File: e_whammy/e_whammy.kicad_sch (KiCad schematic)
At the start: 15 parts, among them J1 I/O connector, U1 HT7550-1, U2 TLV6001UIDBVR, U3 DRV5056

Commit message: Added kikit fab script
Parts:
- RV1: JLCPCB_CORRECTION (none) -> 0;0;270
- U3: JLCPCB_CORRECTION (none) -> 0;0;180
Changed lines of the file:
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@@
       (effects (font (size 1.524 1.524)) hide)
+    )
+    (property "JLCPCB_CORRECTION" "0;0;270" (id 5) (at 117.475 93.98 0)
+      (effects (font (size 1.27 1.27)) hide)
     )
     (pin "1")
@@
       (effects (font (size 1.524 1.524)) hide)
     )
+    (property "JLCPCB_CORRECTION" "0;0;180" (id 5) (at 107.95 118.11 0)
+      (effects (font (size 1.27 1.27)) hide)
+    )
     (pin "1")

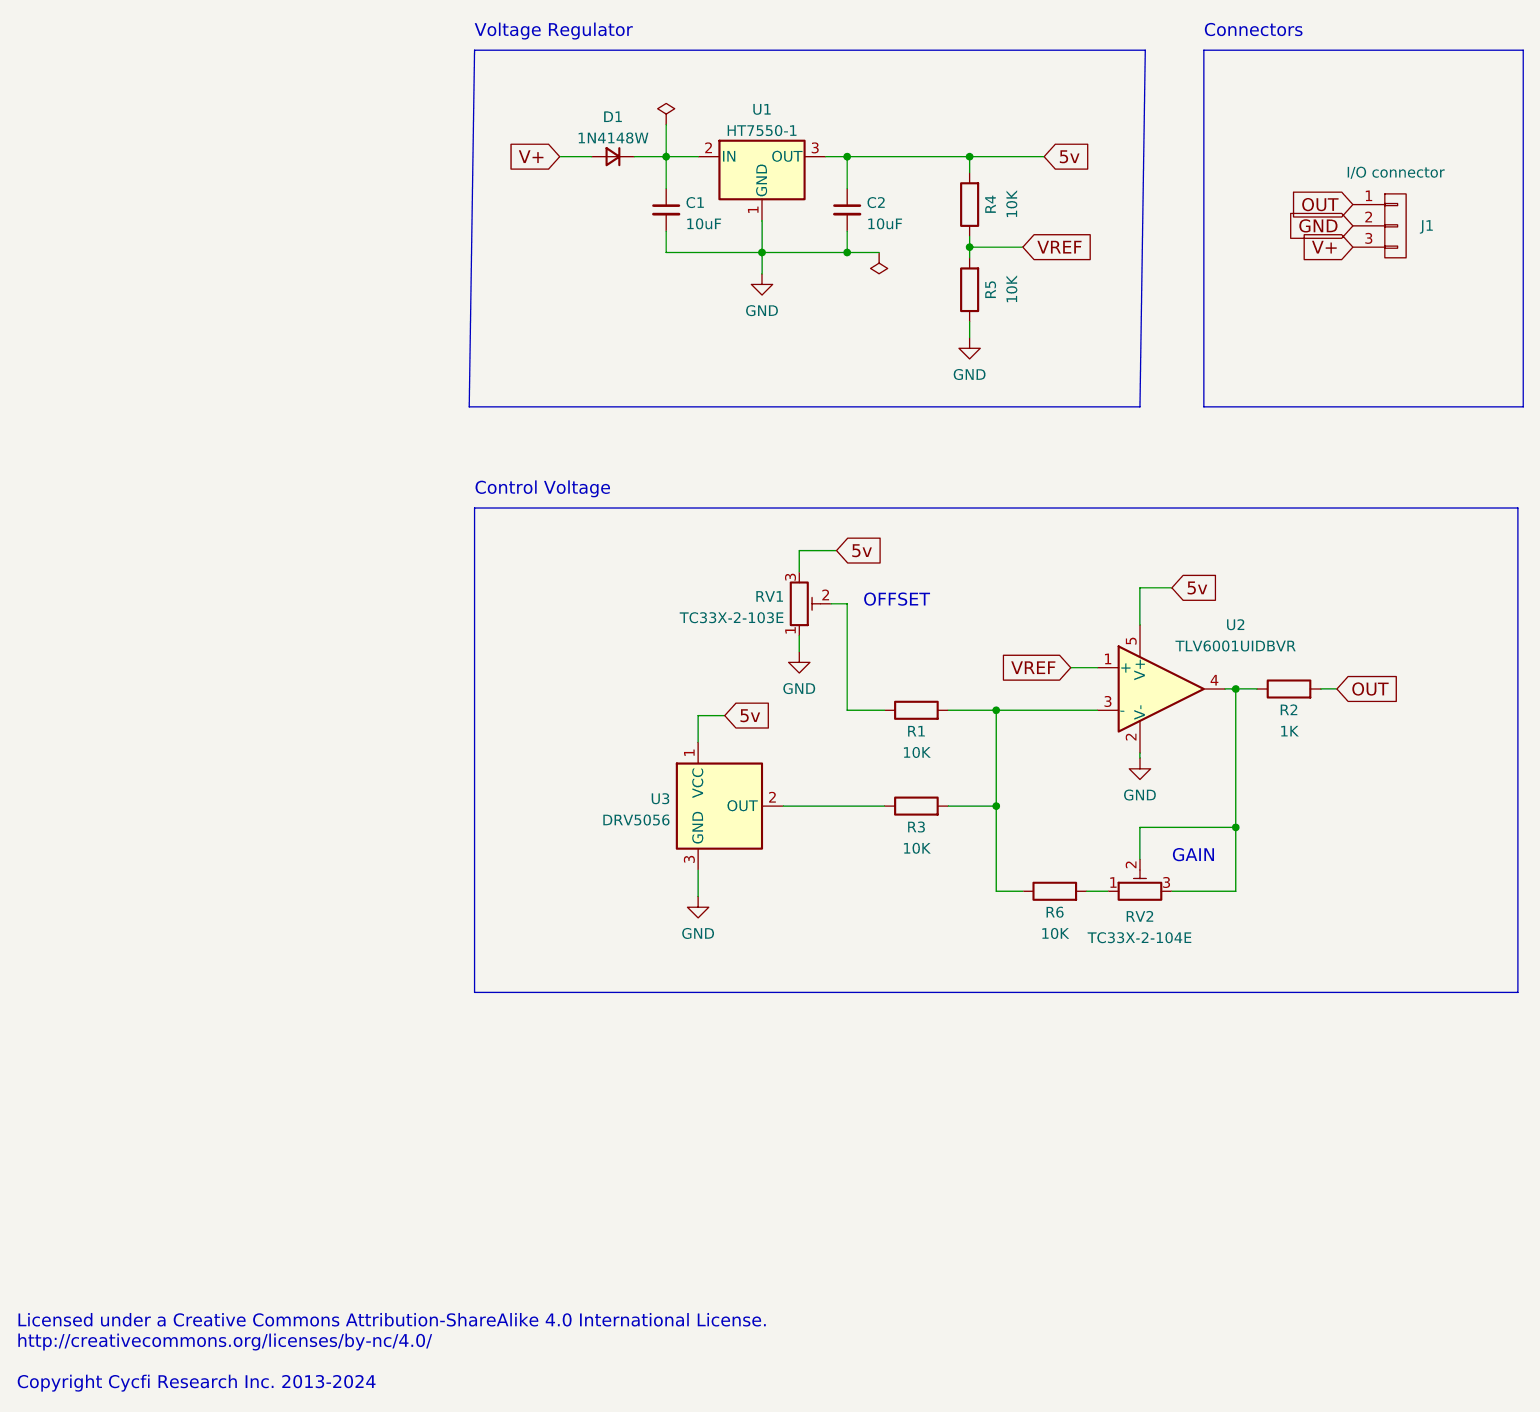
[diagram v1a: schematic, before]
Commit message: Changed to non-inverting configuration
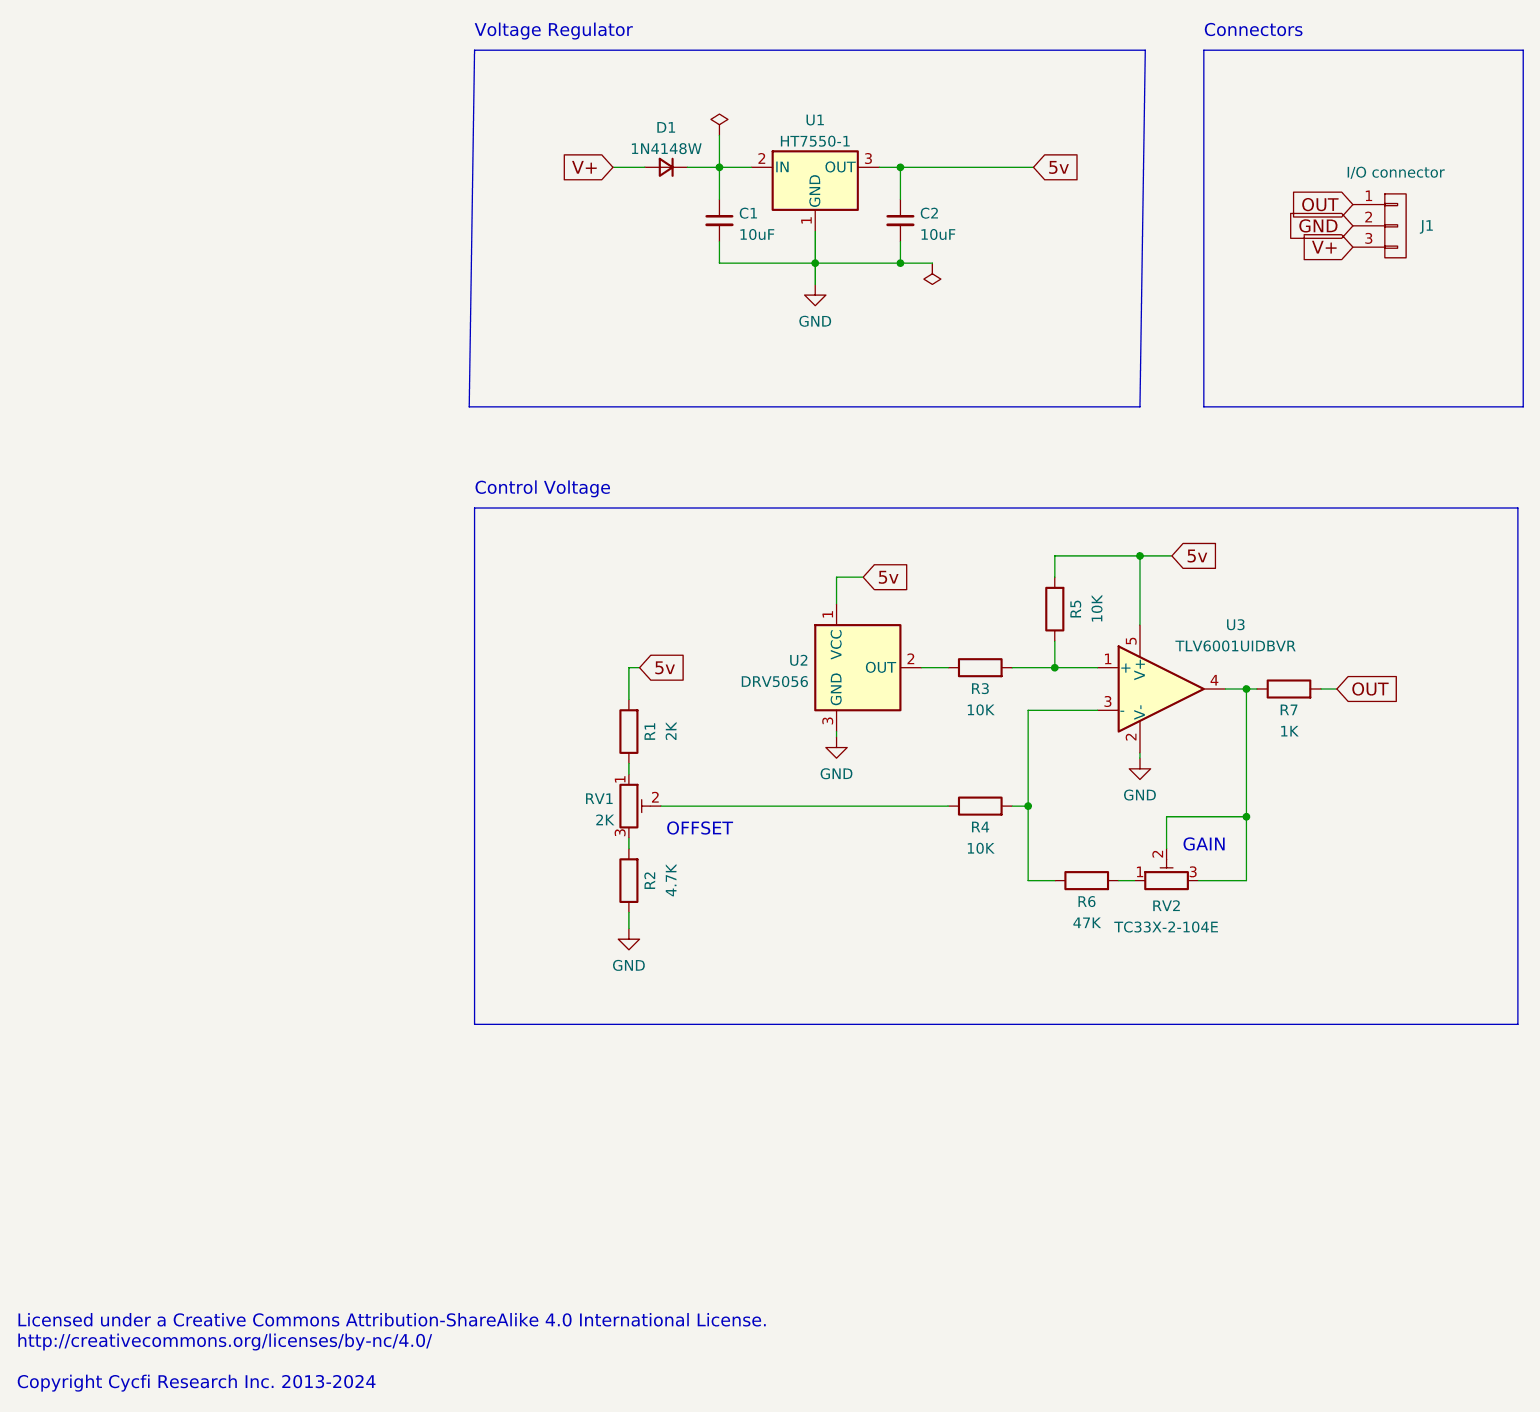
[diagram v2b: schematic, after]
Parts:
- removed R5: 10K, Resistor_SMD:R_0402_1005Metric, symbol Device:R
- added R1: 2K, Resistor_SMD:R_0402_1005Metric, symbol Device:R
- added R6: 47K, Resistor_SMD:R_0402_1005Metric, symbol Device:R
- R2: renamed from R6; value 10K -> 4.7K; LCSC C25744 -> C25900
- RV1: value TC33X-2-103E -> 2K; LCSC C719176 -> C720647
- renumbered R1 to R5, R2 to R7, U3 to U2, U2 to U3
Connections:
- net 5v: now also R5.2, R1.2; no longer R4.2, RV1.3
- net GND: now also R2.1; no longer RV1.1
- net at R5.1: now also R3.2, U3.1 (+); no longer RV1.2
- net at R2.2: now also RV1.3; no longer RV2.1
- net VREF: no longer names the net of R4.1
- net VREF: now also RV1.2; no longer U3.1 (+)
- new net: R1.1, RV1.1
- new net: R6.2, RV2.1
- new net: R4.2, R6.1, U3.3 (-)
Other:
- moved on the sheet: C1, C2, D1, R2, R3, R5, RV1, RV2, U1, U2

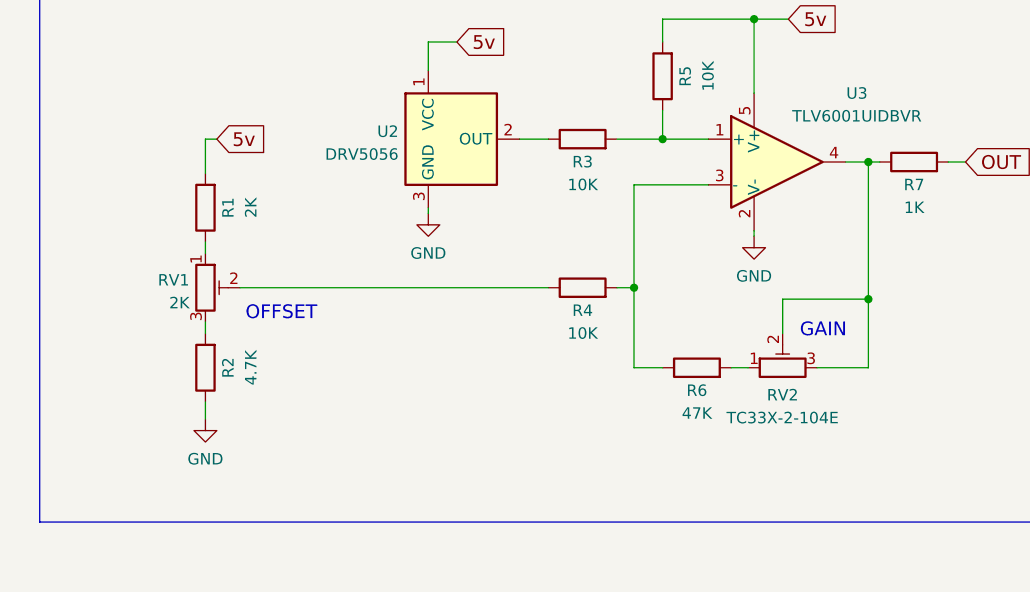
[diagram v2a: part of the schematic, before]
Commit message: Adjusted values for component availability
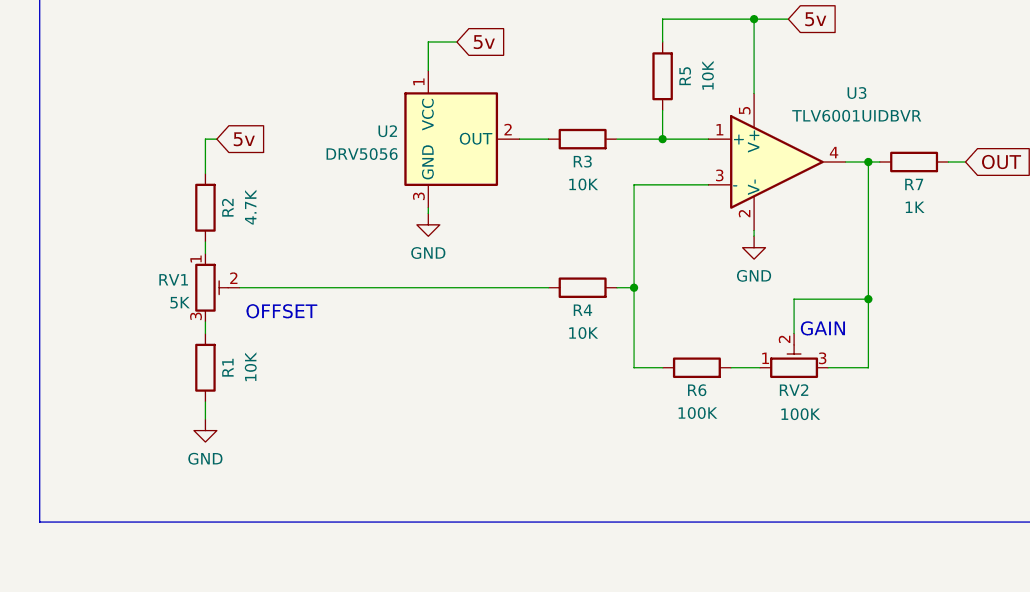
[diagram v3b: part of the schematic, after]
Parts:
- R1: value 2K -> 10K; LCSC C4109 -> C25744
- R6: value 47K -> 100K; LCSC C25792 -> C25741
- RV1: value 2K -> 5K; LCSC C720647 -> C719177
- RV2: value TC33X-2-104E -> 100K
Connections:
- net 5v: now also R2.2; no longer R1.2
- net GND: now also R1.1; no longer R2.1
- net at RV1.1: now also R2.1; no longer R1.1
- net at RV1.3: now also R1.2; no longer R2.2
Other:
- moved on the sheet: R2, RV2
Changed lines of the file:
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@@
   (junction (at 144.78 118.11) (diameter 0) (color 0 0 0 0)
   )
+  (junction (at 119.38 53.34) (diameter 0) (color 0 0 0 0)
+  )
+  (junction (at 129.54 41.91) (diameter 0) (color 0 0 0 0)
+  )
   (junction (at 170.815 119.38) (diameter 0) (color 0 0 0 0)
   )
-  (junction (at 119.38 53.34) (diameter 0) (color 0 0 0 0)
-  )
-  (junction (at 129.54 41.91) (diameter 0) (color 0 0 0 0)
-  )
   (junction (at 147.955 101.6) (diameter 0) (color 0 0 0 0)
   )
@@
     (stroke (width 0) (type default) (color 0 0 0 0))
   )
-  (wire (pts (xy 161.29 123.19) (xy 161.29 119.38))
-    (stroke (width 0) (type default) (color 0 0 0 0))
-  )
   (polyline (pts (xy 165.735 27.94) (xy 203.835 27.94))
     (stroke (width 0) (type default) (color 0 0 0 0))
@@
     (stroke (width 0) (type default) (color 0 0 0 0))
   )
-  (wire (pts (xy 170.815 127) (xy 170.815 119.38))
-    (stroke (width 0) (type default) (color 0 0 0 0))
-  )
-  (wire (pts (xy 165.1 127) (xy 170.815 127))
+  (wire (pts (xy 166.37 127) (xy 170.815 127))
     (stroke (width 0) (type default) (color 0 0 0 0))
   )
@@
     (stroke (width 0) (type default) (color 0 0 0 0))
   )
+  (wire (pts (xy 162.56 119.38) (xy 170.815 119.38))
+    (stroke (width 0) (type default) (color 0 0 0 0))
+  )
   (polyline (pts (xy 78.74 27.94) (xy 78.105 70.485))
     (stroke (width 0) (type default) (color 0 0 0 0))
@@
     (stroke (width 0) (type default) (color 0 0 0 0))
   )
-  (wire (pts (xy 155.575 127) (xy 157.48 127))
+  (wire (pts (xy 155.575 127) (xy 158.75 127))
     (stroke (width 0) (type default) (color 0 0 0 0))
   )
@@
     (stroke (width 0) (type default) (color 0 0 0 0))
   )
-  (wire (pts (xy 161.29 119.38) (xy 170.815 119.38))
-    (stroke (width 0) (type default) (color 0 0 0 0))
-  )
   (wire (pts (xy 97.155 105.41) (xy 97.155 101.6))
     (stroke (width 0) (type default) (color 0 0 0 0))
@@
     (stroke (width 0) (type default) (color 0 0 0 0))
   )
-  (wire (pts (xy 170.815 119.38) (xy 170.815 104.14))
+  (wire (pts (xy 170.815 104.14) (xy 170.815 119.38))
     (stroke (width 0) (type default) (color 0 0 0 0))
   )
@@
     (stroke (width 0) (type default) (color 0 0 0 0))
   )
+  (wire (pts (xy 162.56 123.19) (xy 162.56 119.38))
+    (stroke (width 0) (type default) (color 0 0 0 0))
+  )
   (polyline (pts (xy 158.75 27.94) (xy 158.115 70.485))
     (stroke (width 0) (type default) (color 0 0 0 0))
@@
   )
   (wire (pts (xy 121.92 109.22) (xy 121.92 109.855))
+    (stroke (width 0) (type default) (color 0 0 0 0))
+  )
+  (wire (pts (xy 170.815 119.38) (xy 170.815 127))
     (stroke (width 0) (type default) (color 0 0 0 0))
   )
@@
     (pin "1")
   )
-  (symbol (lib_id "Device:R") (at 97.155 109.22 180) (unit 1)
-    (in_bom yes) (on_board yes)
-    (property "Reference" "R1" (id 0) (at 99.6981 109.22 90))
-    (property "Value" "2K" (id 1) (at 102.235 109.22 90))
-    (property "Footprint" "Resistor_SMD:R_0402_1005Metric" (id 2) (at 98.933 109.22 90)
-      (effects (font (size 1.27 1.27)) hide)
-    )
-    (property "Datasheet" "~" (id 3) (at 97.155 109.22 0)
-      (effects (font (size 1.27 1.27)) hide)
-    )
-    (property "LCSC" "C4109" (id 4) (at 97.155 109.22 0)
-      (effects (font (size 1.524 1.524)) hide)
-    )
-    (pin "1")
-    (pin "2")
-  )
   (symbol (lib_id "Device:R") (at 175.895 104.14 90) (unit 1)
     (in_bom yes) (on_board yes)
@@
     (pin "1")
   )
+  (symbol (lib_id "Device:R") (at 97.155 127 180) (unit 1)
+    (in_bom yes) (on_board yes)
+    (property "Reference" "R1" (id 0) (at 99.6981 127 90))
+    (property "Value" "10K" (id 1) (at 102.235 127 90))
+    (property "Footprint" "Resistor_SMD:R_0402_1005Metric" (id 2) (at 98.933 127 90)
+      (effects (font (size 1.27 1.27)) hide)
+    )
+    (property "Datasheet" "~" (id 3) (at 97.155 127 0)
+      (effects (font (size 1.27 1.27)) hide)
+    )
+    (property "LCSC" "C25744" (id 4) (at 97.155 127 0)
+      (effects (font (size 1.524 1.524)) hide)
+    )
+    (pin "1")
+    (pin "2")
+  )
   (symbol (lib_id "Device:C_Small") (at 107.95 48.26 0) (unit 1)
     (in_bom yes) (on_board yes) (fields_autoplaced)
@@
       (effects (font (size 1.27 1.27)) (justify right))
     )
-    (property "Value" "2K" (id 1) (at 95.3771 119.8122 0)
+    (property "Value" "5K" (id 1) (at 95.3771 119.8122 0)
       (effects (font (size 1.27 1.27)) (justify right))
     )
@@
       (effects (font (size 1.27 1.27)) hide)
     )
-    (property "LCSC" "C720647" (id 4) (at 97.155 118.11 90)
+    (property "LCSC" "C719177" (id 4) (at 97.155 118.11 90)
       (effects (font (size 1.524 1.524)) hide)
     )
@@
     (pin "2")
   )
-  (symbol (lib_id "Device:R_Potentiometer_Trim") (at 161.29 127 90) (unit 1)
-    (in_bom yes) (on_board yes) (fields_autoplaced)
-    (property "Reference" "RV2" (id 0) (at 161.29 130.0464 90))
-    (property "Value" "TC33X-2-104E" (id 1) (at 161.29 132.5833 90))
-    (property "Footprint" "cycfi_library:TC33X-2" (id 2) (at 161.29 127 0)
-      (effects (font (size 1.27 1.27)) hide)
-    )
-    (property "Datasheet" "~" (id 3) (at 161.29 127 0)
-      (effects (font (size 1.27 1.27)) hide)
-    )
-    (property "LCSC" "C719186" (id 4) (at 161.29 127 90)
+  (symbol (lib_id "Device:R_Potentiometer_Trim") (at 162.56 127 90) (unit 1)
+    (in_bom yes) (on_board yes)
+    (property "Reference" "RV2" (id 0) (at 162.56 129.54 90))
+    (property "Value" "100K" (id 1) (at 163.195 132.2086 90))
+    (property "Footprint" "cycfi_library:TC33X-2" (id 2) (at 162.56 127 0)
+      (effects (font (size 1.27 1.27)) hide)
+    )
+    (property "Datasheet" "~" (id 3) (at 162.56 127 0)
+      (effects (font (size 1.27 1.27)) hide)
+    )
+    (property "LCSC" "C719186" (id 4) (at 162.56 127 90)
       (effects (font (size 1.524 1.524)) hide)
     )
@@
     (in_bom yes) (on_board yes)
     (property "Reference" "R6" (id 0) (at 151.765 129.5431 90))
-    (property "Value" "47K" (id 1) (at 151.765 132.08 90))
+    (property "Value" "100K" (id 1) (at 151.765 132.08 90))
     (property "Footprint" "Resistor_SMD:R_0402_1005Metric" (id 2) (at 151.765 128.778 90)
       (effects (font (size 1.27 1.27)) hide)
@@
       (effects (font (size 1.27 1.27)) hide)
     )
-    (property "LCSC" "C25792" (id 4) (at 151.765 127 0)
+    (property "LCSC" "C25741" (id 4) (at 151.765 127 0)
       (effects (font (size 1.524 1.524)) hide)
     )
@@
     (pin "3")
   )
-  (symbol (lib_id "Device:R") (at 97.155 127 180) (unit 1)
-    (in_bom yes) (on_board yes)
-    (property "Reference" "R2" (id 0) (at 99.6981 127 90))
-    (property "Value" "4.7K" (id 1) (at 102.235 127 90))
-    (property "Footprint" "Resistor_SMD:R_0402_1005Metric" (id 2) (at 98.933 127 90)
-      (effects (font (size 1.27 1.27)) hide)
-    )
-    (property "Datasheet" "~" (id 3) (at 97.155 127 0)
-      (effects (font (size 1.27 1.27)) hide)
-    )
-    (property "LCSC" "C25900" (id 4) (at 97.155 127 0)
+  (symbol (lib_id "Device:R") (at 97.155 109.22 180) (unit 1)
+    (in_bom yes) (on_board yes)
+    (property "Reference" "R2" (id 0) (at 99.6981 109.22 90))
+    (property "Value" "4.7K" (id 1) (at 102.235 109.22 90))
+    (property "Footprint" "Resistor_SMD:R_0402_1005Metric" (id 2) (at 98.933 109.22 90)
+      (effects (font (size 1.27 1.27)) hide)
+    )
+    (property "Datasheet" "~" (id 3) (at 97.155 109.22 0)
+      (effects (font (size 1.27 1.27)) hide)
+    )
+    (property "LCSC" "C25900" (id 4) (at 97.155 109.22 0)
       (effects (font (size 1.524 1.524)) hide)
     )
@@
       (reference "J1") (unit 1) (value "I/O connector") (footprint "Connector_PinHeader_2.54mm:PinHeader_1x03_P2.54mm_Vertical")
     )
-    (path "/4e901853-9626-48a3-acc0-afd5e8d0d593"
-      (reference "R1") (unit 1) (value "2K") (footprint "Resistor_SMD:R_0402_1005Metric")
+    (path "/676149e8-29a3-4a98-b7e8-59babd9011af"
+      (reference "R1") (unit 1) (value "10K") (footprint "Resistor_SMD:R_0402_1005Metric")
     )
     (path "/cd7dfa0a-0bf9-44de-b5f2-0f86632ac2bb"
@@
     )
     (path "/b7dcd967-8b03-4bd9-bb8e-f3beb9ae1901"
-      (reference "R6") (unit 1) (value "47K") (footprint "Resistor_SMD:R_0402_1005Metric")
+      (reference "R6") (unit 1) (value "100K") (footprint "Resistor_SMD:R_0402_1005Metric")
     )
     (path "/5d8a21c6-2de7-445f-ab12-c2879dbf2517"
@@
     )
     (path "/86f55a24-72be-4271-a869-bb23db557d60"
-      (reference "RV1") (unit 1) (value "2K") (footprint "cycfi_library:TC33X-2")
+      (reference "RV1") (unit 1) (value "5K") (footprint "cycfi_library:TC33X-2")
     )
     (path "/b1a40886-d232-44d1-8002-9e9deb56b693"
-      (reference "RV2") (unit 1) (value "TC33X-2-104E") (footprint "cycfi_library:TC33X-2")
+      (reference "RV2") (unit 1) (value "100K") (footprint "cycfi_library:TC33X-2")
     )
     (path "/b29e7a3c-8a61-4d5d-8478-053e45b60270"
